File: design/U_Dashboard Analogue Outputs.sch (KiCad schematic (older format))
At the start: 22 parts

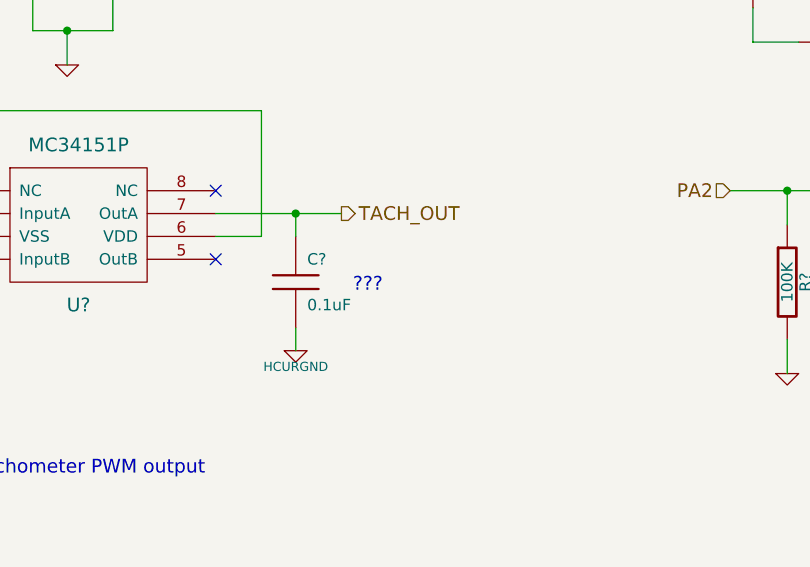
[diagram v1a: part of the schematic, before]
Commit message: decide to put CPU on mainboard, drop core board design
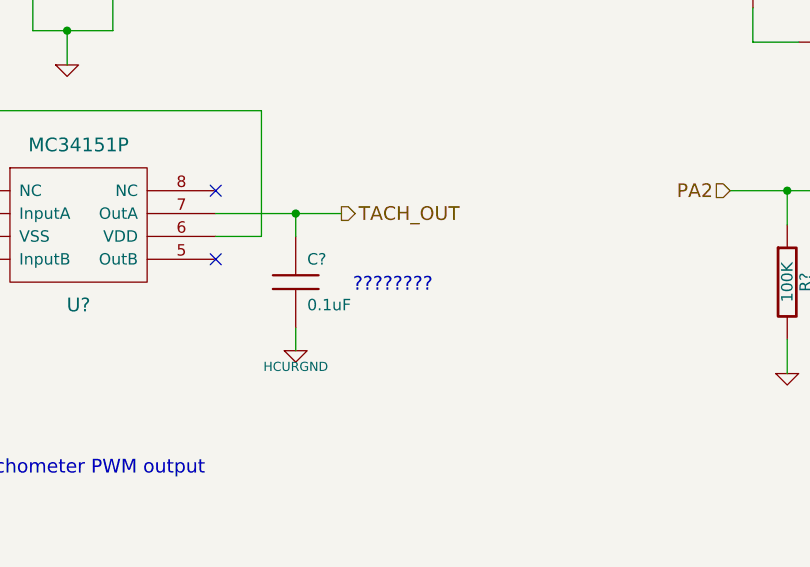
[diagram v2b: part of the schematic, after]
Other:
- note added: "????????"
- note removed: "???"
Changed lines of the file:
@@
-EESchema Schematic File Version 2  date 19/10/2011 09:07:12
+EESchema Schematic File Version 2  date 27/12/2011 00:52:12
 LIBS:power
 LIBS:device
@@
 LIBS:contrib
 LIBS:valves
-LIBS:freeEMS_lib
-LIBS:catsquirt_ioboard-cache
+LIBS:mainboard-cache
 EELAYER 25  0
 EELAYER END
 $Descr A4 11700 8267
-Sheet 3 12
+Sheet 4 12
 Title ""
-Date "19 oct 2011"
+Date "26 dec 2011"
 Rev ""
 Comp ""
@@
 $EndComp
 Text Notes 4800 3150 0    60   ~ 0
-???
+????????
 Text Notes 3150 3950 0    60   ~ 0
 tachometer PWM output

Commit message: revise schema to be full pin compatible with stock ECU
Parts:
- removed C?: 0.1uF, symbol C
- added C27: ??, symbol C
- R27: renamed from R?; value R -> 220R
- gave numbers to parts that had none: 20
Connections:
- net labels added: LSGND
- net labels removed: HCURGND
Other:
- note removed: "????????"

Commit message: add test points on critical output, resolve all kind of DRC issue, generate a netlist
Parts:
- added W2: TEST, symbol TEST
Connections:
- wire segments 50 -> 63
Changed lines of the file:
@@
-EESchema Schematic File Version 2  date 02/01/2012 14:25:41
+EESchema Schematic File Version 2  date 03/01/2012 09:04:48
 LIBS:power
 LIBS:device
@@
 Sheet 5 12
 Title "Analogue output"
-Date "2 jan 2012"
+Date "3 jan 2012"
 Rev "0.01"
 Comp "diyefi.org"
@@
 Comment4 ""
 $EndDescr
+Wire Wire Line
+	4900 3550 4900 3350
 Connection ~ 4550 2800
 Wire Wire Line
@@
 Connection ~ 2550 2800
 Wire Wire Line
-	2750 5850 3100 5850
+	3100 5850 3000 5850
+Wire Wire Line
+	3000 5850 2750 5850
 Wire Wire Line
 	3550 4750 3450 4750
@@
 	3600 5850 3800 5850
 Wire Wire Line
-	4100 5450 4100 5650
+	4100 5650 4100 5550
+Wire Wire Line
+	4100 5550 4100 5450
 Wire Wire Line
 	4550 4900 4550 4800
@@
 	4100 4750 4100 5050
 Wire Wire Line
-	6800 2700 6450 2700
-Wire Wire Line
-	4000 1400 3100 1400
+	6450 2700 6700 2700
+Wire Wire Line
+	6700 2700 6800 2700
+Wire Wire Line
+	4000 1400 3750 1400
+Wire Wire Line
+	3750 1400 3400 1400
+Wire Wire Line
+	3400 1400 3100 1400
 Connection ~ 3750 1400
 Connection ~ 3400 1400
@@
 Connection ~ 7800 2250
 Wire Wire Line
-	7800 2050 7800 2500
+	7800 2500 7800 2250
+Wire Wire Line
+	7800 2250 7800 2050
 Wire Wire Line
 	8000 2250 7800 2250
@@
 	3400 1800 3400 2000
 Wire Wire Line
-	3400 2000 3750 2000
+	3400 2000 3550 2000
+Wire Wire Line
+	3550 2000 3750 2000
 Wire Wire Line
 	3750 2000 3750 1800
@@
 	2850 2900 2850 3400
 Wire Wire Line
-	4750 2800 4200 2800
-Wire Wire Line
-	7000 5350 6700 5350
+	4200 2800 4550 2800
+Wire Wire Line
+	4550 2800 4900 2800
+Wire Wire Line
+	6700 5350 6900 5350
+Wire Wire Line
+	6900 5350 7000 5350
 Wire Wire Line
 	7950 5550 7950 5750
@@
 	7950 5950 7950 6300
 Wire Wire Line
-	2550 2600 2550 2950
-Wire Wire Line
-	2300 2800 3000 2800
+	2550 2950 2550 2800
+Wire Wire Line
+	2550 2800 2550 2600
+Wire Wire Line
+	3000 2800 2550 2800
+Wire Wire Line
+	2550 2800 2300 2800
 Wire Wire Line
 	3000 6050 3000 5850
@@
 Wire Wire Line
 	4550 3550 4550 3350
-$Comp
-L GND #PWR043
+Wire Wire Line
+	4900 2800 4900 2950
+$Comp
+L GND #PWR52
+U 1 1 4F0253FB
+P 4900 3550
+F 0 "#PWR52" H 4900 3550 30  0001 C CNN
+F 1 "GND" H 4900 3480 30  0001 C CNN
+	1    4900 3550
+	1    0    0    -1
+$EndComp
+$Comp
+L TEST W2
+U 1 1 4F0253AC
+P 4900 3150
+F 0 "W2" H 4900 3210 40  0000 C CNN
+F 1 "TEST" H 4900 3080 40  0000 C CNN
+	1    4900 3150
+	0    1    1    0
+$EndComp
+$Comp
+L GND #PWR51
 U 1 1 4F01410C
 P 4550 3550
-F 0 "#PWR043" H 4550 3550 30  0001 C CNN
+F 0 "#PWR51" H 4550 3550 30  0001 C CNN
 F 1 "GND" H 4550 3480 30  0001 C CNN
 	1    4550 3550
@@
 $EndComp
 $Comp
-L GND #PWR044
+L GND #PWR58
 U 1 1 4F00971C
 P 7950 6300
-F 0 "#PWR044" H 7950 6300 30  0001 C CNN
+F 0 "#PWR58" H 7950 6300 30  0001 C CNN
 F 1 "GND" H 7950 6230 30  0001 C CNN
 	1    7950 6300
@@
 $EndComp
 $Comp
-L GND #PWR045
+L GND #PWR57
 U 1 1 4F0095F8
 P 4100 6300
-F 0 "#PWR045" H 4100 6300 30  0001 C CNN
+F 0 "#PWR57" H 4100 6300 30  0001 C CNN
 F 1 "GND" H 4100 6230 30  0001 C CNN
 	1    4100 6300
@@
 $EndComp
 $Comp
-L LSGND #PWR046
+L LSGND #PWR47
 U 1 1 4F008DFA
 P 7800 3150
-F 0 "#PWR046" H 7800 3150 40  0001 C CNN
+F 0 "#PWR47" H 7800 3150 40  0001 C CNN
 F 1 "LSGND" H 7800 3080 40  0000 C CNN
 	1    7800 3150
@@
 $EndComp
 $Comp
-L GND #PWR047
+L GND #PWR49
 U 1 1 4E946A7A
 P 6700 3500
-F 0 "#PWR047" H 6700 3500 30  0001 C CNN
+F 0 "#PWR49" H 6700 3500 30  0001 C CNN
 F 1 "GND" H 6700 3430 30  0001 C CNN
 	1    6700 3500
@@
 $EndComp
 $Comp
-L GND #PWR048
+L GND #PWR59
 U 1 1 4E946A34
 P 3000 6700
-F 0 "#PWR048" H 3000 6700 30  0001 C CNN
+F 0 "#PWR59" H 3000 6700 30  0001 C CNN
 F 1 "GND" H 3000 6630 30  0001 C CNN
 	1    3000 6700
@@
 $EndComp
 $Comp
-L GND #PWR049
+L GND #PWR56
 U 1 1 4E946A2F
 P 6900 6200
-F 0 "#PWR049" H 6900 6200 30  0001 C CNN
+F 0 "#PWR56" H 6900 6200 30  0001 C CNN
 F 1 "GND" H 6900 6130 30  0001 C CNN
 	1    6900 6200
@@
 PA2
 $Comp
-L GND #PWR050
+L GND #PWR50
 U 1 1 4E9467CA
 P 2550 3550
-F 0 "#PWR050" H 2550 3550 30  0001 C CNN
+F 0 "#PWR50" H 2550 3550 30  0001 C CNN
 F 1 "GND" H 2550 3480 30  0001 C CNN
 	1    2550 3550
@@
 NoConn ~ 3000 3000
 $Comp
-L +12V_SWITCHED #PWR051
+L +12V_SWITCHED #PWR54
 U 1 1 4E94525A
 P 4550 4800
-F 0 "#PWR051" H 4550 4750 20  0001 C CNN
+F 0 "#PWR54" H 4550 4750 20  0001 C CNN
 F 1 "+12V_SWITCHED" H 4550 4900 30  0000 C CNN
 	1    4550 4800
@@
 $EndComp
 $Comp
-L +12V_SWITCHED #PWR052
+L +12V_SWITCHED #PWR53
 U 1 1 4E94523D
 P 3450 4650
-F 0 "#PWR052" H 3450 4600 20  0001 C CNN
+F 0 "#PWR53" H 3450 4600 20  0001 C CNN
 F 1 "+12V_SWITCHED" H 3450 4750 30  0000 C CNN
 	1    3450 4650
@@
 PA3
 $Comp
-L GND #PWR053
+L GND #PWR48
 U 1 1 4E941220
 P 2850 3400
-F 0 "#PWR053" H 2850 3400 30  0001 C CNN
+F 0 "#PWR48" H 2850 3400 30  0001 C CNN
 F 1 "GND" H 2850 3330 30  0001 C CNN
 	1    2850 3400
@@
 $EndComp
 $Comp
-L +12V_SWITCHED #PWR054
+L +12V_SWITCHED #PWR43
 U 1 1 4E9411EA
 P 4650 1300
-F 0 "#PWR054" H 4650 1250 20  0001 C CNN
+F 0 "#PWR43" H 4650 1250 20  0001 C CNN
 F 1 "+12V_SWITCHED" H 4650 1400 30  0000 C CNN
 	1    4650 1300
@@
 $EndComp
 $Comp
-L +5V_SWITCHED #PWR055
+L +5V_SWITCHED #PWR55
 U 1 1 4E93D9D9
 P 7950 4850
-F 0 "#PWR055" H 7950 4800 20  0001 C CNN
+F 0 "#PWR55" H 7950 4800 20  0001 C CNN
 F 1 "+5V_SWITCHED" H 7950 4950 30  0000 C CNN
 	1    7950 4850
@@
 $EndComp
 $Comp
-L +5V_SWITCHED #PWR056
+L +5V_SWITCHED #PWR45
 U 1 1 4E93D8FC
 P 2550 1950
-F 0 "#PWR056" H 2550 1900 20  0001 C CNN
+F 0 "#PWR45" H 2550 1900 20  0001 C CNN
 F 1 "+5V_SWITCHED" H 2550 2050 30  0000 C CNN
 	1    2550 1950
@@
 $EndComp
 $Comp
-L +12V_SWITCHED #PWR057
+L +12V_SWITCHED #PWR44
 U 1 1 4E93D9A2
 P 6550 1900
-F 0 "#PWR057" H 6550 1850 20  0001 C CNN
+F 0 "#PWR44" H 6550 1850 20  0001 C CNN
 F 1 "+12V_SWITCHED" H 6550 2000 30  0000 C CNN
 	1    6550 1900
@@
 	1    0    0    -1
 $EndComp
-Text HLabel 4750 2800 2    60   Output ~ 0
+Text HLabel 4900 2800 2    60   Output ~ 0
 TACH_OUT
 $Comp
@@
 $EndComp
 $Comp
-L GND #PWR058
+L GND #PWR46
 U 1 1 4E939C41
 P 3550 2150
-F 0 "#PWR058" H 3550 2150 30  0001 C CNN
+F 0 "#PWR46" H 3550 2150 30  0001 C CNN
 F 1 "GND" H 3550 2080 30  0001 C CNN
 	1    3550 2150

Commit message: add missing diodes, re-generate netlist, assign all footprints, ready to layout
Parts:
- added D13: DIODE, symbol DIODE
- Q1: value MOS_N -> vnp10n07
- renumbered D13 to D14
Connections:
- wire segments 63 -> 54
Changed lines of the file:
@@
-EESchema Schematic File Version 2  date 03/01/2012 09:04:48
+EESchema Schematic File Version 2  date 12/01/2012 20:05:35
 LIBS:power
 LIBS:device
@@
 Sheet 5 12
 Title "Analogue output"
-Date "3 jan 2012"
+Date "12 jan 2012"
 Rev "0.01"
 Comp "diyefi.org"
@@
 $EndDescr
 Wire Wire Line
+	8050 2900 7800 2900
+Wire Wire Line
 	4900 3550 4900 3350
 Connection ~ 4550 2800
@@
 Connection ~ 2550 2800
 Wire Wire Line
-	3100 5850 3000 5850
-Wire Wire Line
-	3000 5850 2750 5850
+	3100 5850 2750 5850
 Wire Wire Line
 	3550 4750 3450 4750
@@
 	3600 5850 3800 5850
 Wire Wire Line
-	4100 5650 4100 5550
-Wire Wire Line
-	4100 5550 4100 5450
+	4100 5650 4100 5450
 Wire Wire Line
 	4550 4900 4550 4800
@@
 	4100 4750 4100 5050
 Wire Wire Line
-	6450 2700 6700 2700
-Wire Wire Line
-	6700 2700 6800 2700
-Wire Wire Line
-	4000 1400 3750 1400
-Wire Wire Line
-	3750 1400 3400 1400
-Wire Wire Line
-	3400 1400 3100 1400
+	6450 2700 6800 2700
+Wire Wire Line
+	4000 1400 3100 1400
 Connection ~ 3750 1400
 Connection ~ 3400 1400
@@
 Connection ~ 7800 2250
 Wire Wire Line
-	7800 2500 7800 2250
-Wire Wire Line
-	7800 2250 7800 2050
+	7800 2050 7800 2500
 Wire Wire Line
 	8000 2250 7800 2250
@@
 	3400 1800 3400 2000
 Wire Wire Line
-	3400 2000 3550 2000
-Wire Wire Line
-	3550 2000 3750 2000
+	3400 2000 3750 2000
 Wire Wire Line
 	3750 2000 3750 1800
@@
 	2850 2900 2850 3400
 Wire Wire Line
-	4200 2800 4550 2800
-Wire Wire Line
-	4550 2800 4900 2800
-Wire Wire Line
-	6700 5350 6900 5350
-Wire Wire Line
-	6900 5350 7000 5350
+	4200 2800 4900 2800
+Wire Wire Line
+	6700 5350 7000 5350
 Wire Wire Line
 	7950 5550 7950 5750
@@
 	7950 5950 7950 6300
 Wire Wire Line
-	2550 2950 2550 2800
-Wire Wire Line
-	2550 2800 2550 2600
-Wire Wire Line
-	3000 2800 2550 2800
-Wire Wire Line
-	2550 2800 2300 2800
+	2550 2950 2550 2600
+Wire Wire Line
+	3000 2800 2300 2800
 Wire Wire Line
 	3000 6050 3000 5850
@@
 Wire Wire Line
 	4900 2800 4900 2950
+Wire Wire Line
+	7800 2500 8050 2500
+$Comp
+L DIODE D13
+U 1 1 4F0EC9C3
+P 8050 2700
+F 0 "D13" H 8050 2800 40  0000 C CNN
+F 1 "DIODE" H 8050 2600 40  0000 C CNN
+	1    8050 2700
+	0    -1   -1   0
+$EndComp
 $Comp
 L GND #PWR52
@@
 $EndComp
 $Comp
-L LED D13
+L LED D14
 U 1 1 4E941A01
 P 4100 5250
-F 0 "D13" H 4100 5350 50  0000 C CNN
+F 0 "D14" H 4100 5350 50  0000 C CNN
 F 1 "LED" H 4100 5150 50  0000 C CNN
 	1    4100 5250
@@
 P 7700 2700
 F 0 "Q1" H 7710 2870 60  0000 R CNN
-F 1 "MOS_N" H 7710 2550 60  0000 R CNN
+F 1 "vnp10n07" H 7710 2550 60  0000 R CNN
 	1    7700 2700
 	1    0    0    -1

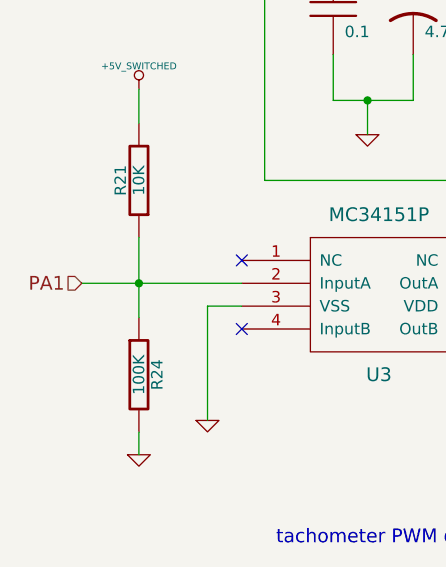
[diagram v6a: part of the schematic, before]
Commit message: use max9924 to replace ncv1124, add narrow band oxygen sensor differential input circuit, put all component into PCB edge
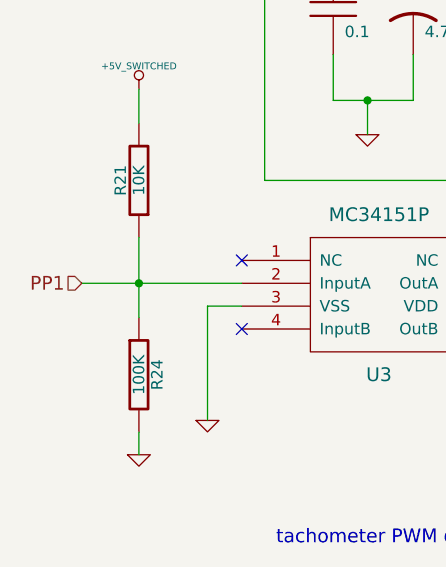
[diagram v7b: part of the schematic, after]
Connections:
- net labels added: PP1
- net labels removed: PA1
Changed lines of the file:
@@
-EESchema Schematic File Version 2  date 14/01/2012 13:46:11
+EESchema Schematic File Version 2  date 21/01/2012 01:12:26
 LIBS:power
 LIBS:device
@@
 LIBS:contrib
 LIBS:valves
+LIBS:freeEMS_lib
 LIBS:mainboard-cache
 EELAYER 25  0
 EELAYER END
 $Descr A4 11700 8267
-Sheet 5 12
+Sheet 3 12
 Title "Analogue output"
-Date "14 jan 2012"
+Date "20 jan 2012"
 Rev "0.01"
 Comp "diyefi.org"
@@
 $EndComp
 $Comp
-L GND #PWR52
+L GND #PWR15
 U 1 1 4F0253FB
 P 4900 3550
-F 0 "#PWR52" H 4900 3550 30  0001 C CNN
+F 0 "#PWR15" H 4900 3550 30  0001 C CNN
 F 1 "GND" H 4900 3480 30  0001 C CNN
 	1    4900 3550
@@
 $EndComp
 $Comp
-L GND #PWR51
+L GND #PWR14
 U 1 1 4F01410C
 P 4550 3550
-F 0 "#PWR51" H 4550 3550 30  0001 C CNN
+F 0 "#PWR14" H 4550 3550 30  0001 C CNN
 F 1 "GND" H 4550 3480 30  0001 C CNN
 	1    4550 3550
@@
 $EndComp
 $Comp
-L GND #PWR58
+L GND #PWR21
 U 1 1 4F00971C
 P 7950 6300
-F 0 "#PWR58" H 7950 6300 30  0001 C CNN
+F 0 "#PWR21" H 7950 6300 30  0001 C CNN
 F 1 "GND" H 7950 6230 30  0001 C CNN
 	1    7950 6300
@@
 $EndComp
 $Comp
-L GND #PWR57
+L GND #PWR20
 U 1 1 4F0095F8
 P 4100 6300
-F 0 "#PWR57" H 4100 6300 30  0001 C CNN
+F 0 "#PWR20" H 4100 6300 30  0001 C CNN
 F 1 "GND" H 4100 6230 30  0001 C CNN
 	1    4100 6300
@@
 $EndComp
 $Comp
-L LSGND #PWR47
+L LSGND #PWR10
 U 1 1 4F008DFA
 P 7800 3150
-F 0 "#PWR47" H 7800 3150 40  0001 C CNN
+F 0 "#PWR10" H 7800 3150 40  0001 C CNN
 F 1 "LSGND" H 7800 3080 40  0000 C CNN
 	1    7800 3150
@@
 $EndComp
 $Comp
-L GND #PWR49
+L GND #PWR12
 U 1 1 4E946A7A
 P 6700 3500
-F 0 "#PWR49" H 6700 3500 30  0001 C CNN
+F 0 "#PWR12" H 6700 3500 30  0001 C CNN
 F 1 "GND" H 6700 3430 30  0001 C CNN
 	1    6700 3500
@@
 $EndComp
 $Comp
-L GND #PWR59
+L GND #PWR22
 U 1 1 4E946A34
 P 3000 6700
-F 0 "#PWR59" H 3000 6700 30  0001 C CNN
+F 0 "#PWR22" H 3000 6700 30  0001 C CNN
 F 1 "GND" H 3000 6630 30  0001 C CNN
 	1    3000 6700
@@
 $EndComp
 $Comp
-L GND #PWR56
+L GND #PWR19
 U 1 1 4E946A2F
 P 6900 6200
-F 0 "#PWR56" H 6900 6200 30  0001 C CNN
+F 0 "#PWR19" H 6900 6200 30  0001 C CNN
 F 1 "GND" H 6900 6130 30  0001 C CNN
 	1    6900 6200
@@
 PA2
 $Comp
-L GND #PWR50
+L GND #PWR13
 U 1 1 4E9467CA
 P 2550 3550
-F 0 "#PWR50" H 2550 3550 30  0001 C CNN
+F 0 "#PWR13" H 2550 3550 30  0001 C CNN
 F 1 "GND" H 2550 3480 30  0001 C CNN
 	1    2550 3550
@@
 $EndComp
 Text HLabel 2300 2800 0    60   Input ~ 0
-PA1
+PP1
 $Comp
 L R R24
@@
 NoConn ~ 3000 3000
 $Comp
-L +12V_SWITCHED #PWR54
+L +12V_SWITCHED #PWR17
 U 1 1 4E94525A
 P 4550 4800
-F 0 "#PWR54" H 4550 4750 20  0001 C CNN
+F 0 "#PWR17" H 4550 4750 20  0001 C CNN
 F 1 "+12V_SWITCHED" H 4550 4900 30  0000 C CNN
 	1    4550 4800
@@
 $EndComp
 $Comp
-L +12V_SWITCHED #PWR53
+L +12V_SWITCHED #PWR16
 U 1 1 4E94523D
 P 3450 4650
-F 0 "#PWR53" H 3450 4600 20  0001 C CNN
+F 0 "#PWR16" H 3450 4600 20  0001 C CNN
 F 1 "+12V_SWITCHED" H 3450 4750 30  0000 C CNN
 	1    3450 4650
@@
 PA3
 $Comp
-L GND #PWR48
+L GND #PWR11
 U 1 1 4E941220
 P 2850 3400
-F 0 "#PWR48" H 2850 3400 30  0001 C CNN
+F 0 "#PWR11" H 2850 3400 30  0001 C CNN
 F 1 "GND" H 2850 3330 30  0001 C CNN
 	1    2850 3400
@@
 $EndComp
 $Comp
-L +12V_SWITCHED #PWR43
+L +12V_SWITCHED #PWR6
 U 1 1 4E9411EA
 P 4650 1300
-F 0 "#PWR43" H 4650 1250 20  0001 C CNN
+F 0 "#PWR6" H 4650 1250 20  0001 C CNN
 F 1 "+12V_SWITCHED" H 4650 1400 30  0000 C CNN
 	1    4650 1300
@@
 $EndComp
 $Comp
-L +5V_SWITCHED #PWR55
+L +5V_SWITCHED #PWR18
 U 1 1 4E93D9D9
 P 7950 4850
-F 0 "#PWR55" H 7950 4800 20  0001 C CNN
+F 0 "#PWR18" H 7950 4800 20  0001 C CNN
 F 1 "+5V_SWITCHED" H 7950 4950 30  0000 C CNN
 	1    7950 4850
@@
 $EndComp
 $Comp
-L +5V_SWITCHED #PWR45
+L +5V_SWITCHED #PWR8
 U 1 1 4E93D8FC
 P 2550 1950
-F 0 "#PWR45" H 2550 1900 20  0001 C CNN
+F 0 "#PWR8" H 2550 1900 20  0001 C CNN
 F 1 "+5V_SWITCHED" H 2550 2050 30  0000 C CNN
 	1    2550 1950
@@
 $EndComp
 $Comp
-L +12V_SWITCHED #PWR44
+L +12V_SWITCHED #PWR7
 U 1 1 4E93D9A2
 P 6550 1900
-F 0 "#PWR44" H 6550 1850 20  0001 C CNN
+F 0 "#PWR7" H 6550 1850 20  0001 C CNN
 F 1 "+12V_SWITCHED" H 6550 2000 30  0000 C CNN
 	1    6550 1900
@@
 $EndComp
 $Comp
-L GND #PWR46
+L GND #PWR9
 U 1 1 4E939C41
 P 3550 2150
-F 0 "#PWR46" H 3550 2150 30  0001 C CNN
+F 0 "#PWR9" H 3550 2150 30  0001 C CNN
 F 1 "GND" H 3550 2080 30  0001 C CNN
 	1    3550 2150

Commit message: make new footprint for max9924 & lm9040, add can bus interface, generate new netlist
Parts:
- removed R26: 1K-1/4W, symbol R
- R25: value 330-1/4W -> 330
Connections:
- wire segments 54 -> 51
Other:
- moved on the sheet: D14, R25, R30
